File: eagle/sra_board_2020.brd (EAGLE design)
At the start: 81.4 x 109.8 mm, 45 parts, among them Q2 IRF9530, SW1 DTS-6, SW2 DTS-6, SW3 DTS-6, SW4 DTS-6, U1 ESP32-DEVKITC-32D, X1 057-006-1

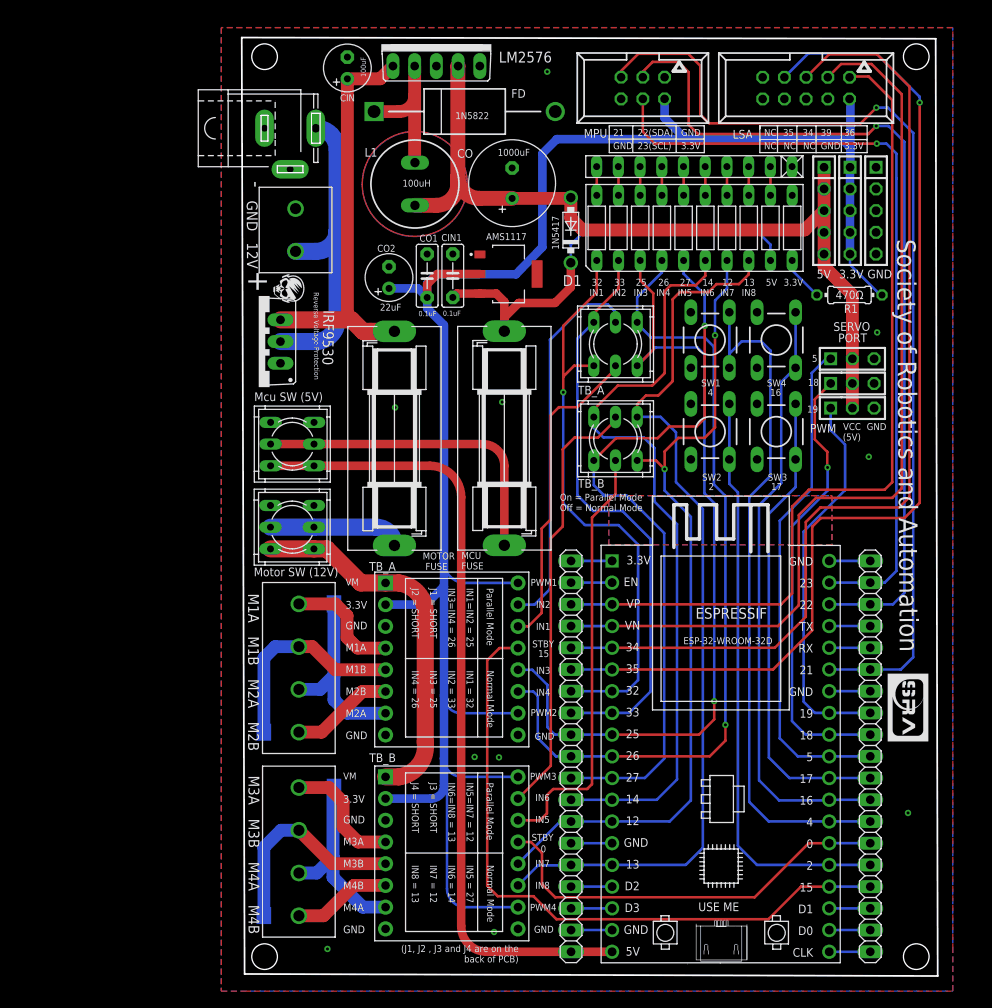
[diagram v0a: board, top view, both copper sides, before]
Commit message: Renamed Eagle files and Added Series Resistor Between ESP and Motor Driver
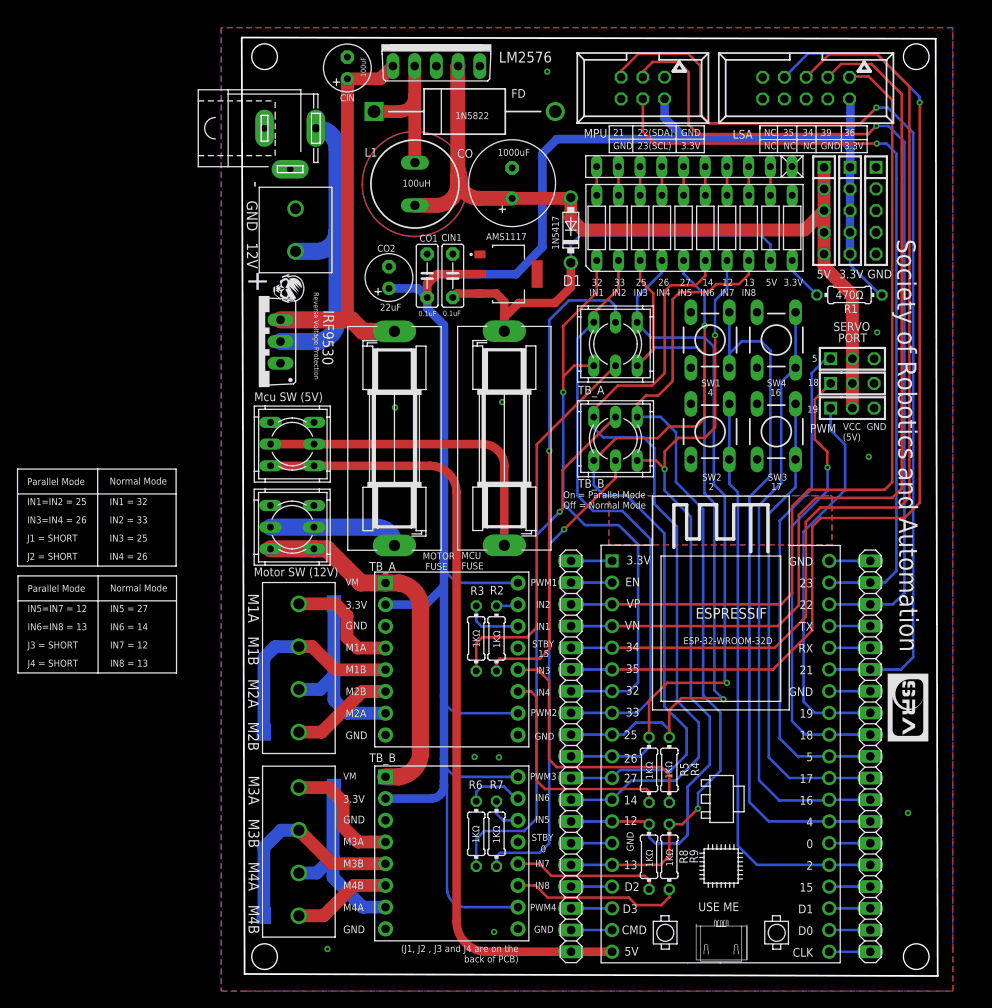
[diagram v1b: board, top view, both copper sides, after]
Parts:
- added R2, R3, R4, R5, R6, R7, R8, R9: 1KΩ, rcl:0204/7
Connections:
- new net N$10: R9.1, TB2.BIN2
- new net N$3: R2.1, TB1.AIN2
- new net N$4: R3.1, TB1.AIN1
- new net N$5: R4.1, TB1.BIN1
- new net N$6: R5.1, TB1.BIN2
- new net N$7: R6.1, TB2.AIN2
- new net N$8: R7.1, TB2.AIN1
- new net N$9: R8.1, TB2.BIN1
- net 12: now also R8.2; no longer TB2.BIN1
- net 13: now also R9.2; no longer TB2.BIN2
- net 15: no longer TB1.STBY
- net 25: now also R4.2; no longer TB1.BIN1
- net 26: now also R5.2; no longer TB1.BIN2
- net AIN1: now also R3.2; no longer TB1.AIN1
- net AIN2: now also R2.2; no longer TB1.AIN2
- net BIN1: now also R7.2; no longer TB2.AIN1
- net BIN2: now also R6.2; no longer TB2.AIN2
- net O: no longer TB2.STBY
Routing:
- net 15: track 78.6 -> 4.80 mm
- net O: track 48.6 -> 4.80 mm
- net N$5: track 0.00 -> 31.4 mm
- net N$6: track 0.00 -> 27.2 mm
- net AMS_IN: track 29.3 -> 50.4 mm
- net N$10: track 0.00 -> 19.9 mm
- net N$9: track 0.00 -> 17.2 mm
- net 26: track 96.4 -> 83.6 mm
- net AIN2: track 44.6 -> 57.2 mm, vias 0 -> 1
- net BIN2: track 51.0 -> 62.0 mm, vias 0 -> 1
- net AIN1: track 37.2 -> 45.5 mm
- net 25: track 95.7 -> 87.5 mm
- net N$4: track 0.00 -> 6.93 mm
- net N$7: track 0.00 -> 6.81 mm
- net 13: track 106.7 -> 100.4 mm, vias 0 -> 1
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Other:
- board text added: "CMD"

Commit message: Change the placement of Series Resistors and cleaned the routing
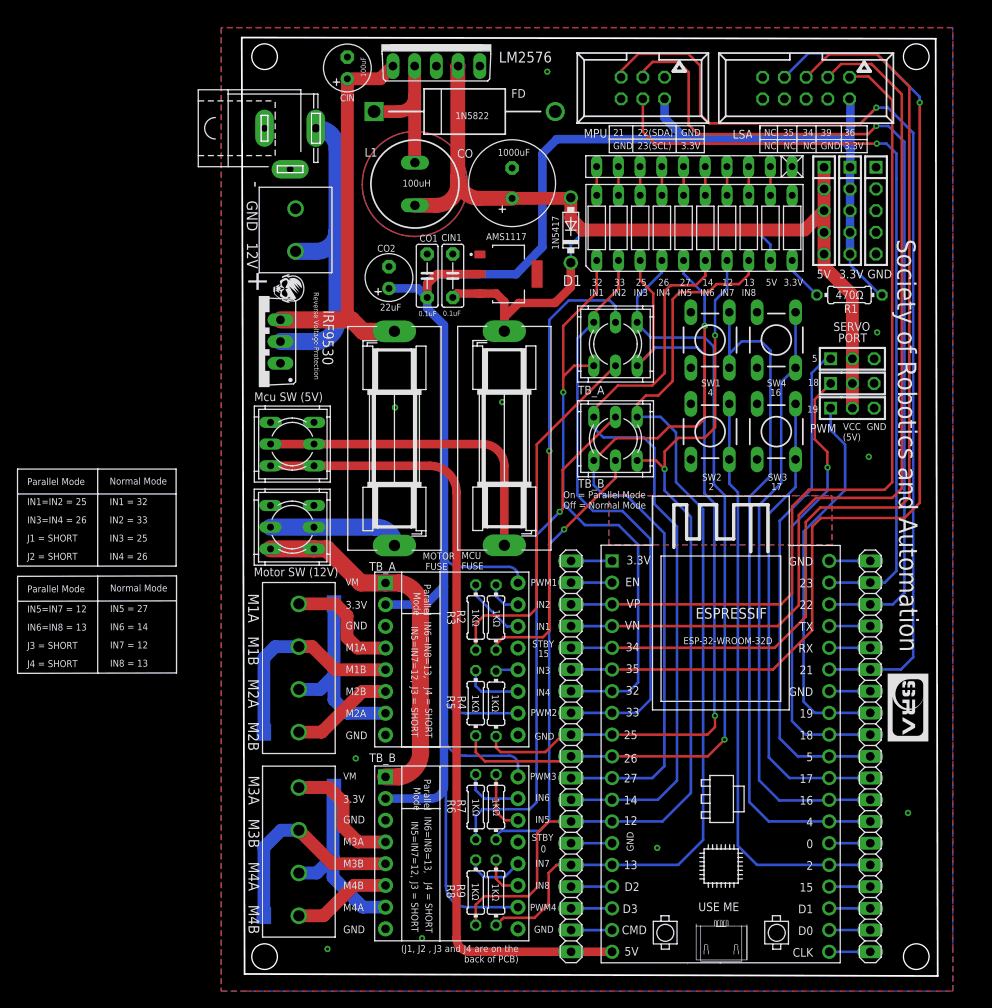
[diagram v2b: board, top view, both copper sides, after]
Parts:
- moved R5 21.7 mm to (27.9, 32.4), turned to 270 degrees
- moved R4 21.7 mm to (30.2, 32.4), turned to 270 degrees
- moved R8 20.7 mm to (27.9, 10.3), turned to 270 degrees
- moved R9 20.7 mm to (30.2, 10.3), turned to 270 degrees
- moved R6 3.13 mm to (27.9, 20.3)
- moved R7 3.13 mm to (30.2, 20.3)
- moved R2 2.45 mm to (30.2, 42.5)
- moved R3 2.45 mm to (27.9, 42.5)
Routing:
- net N$5: track 31.4 -> 2.64 mm
- net N$6: track 27.2 -> 7.01 mm
- net N$10: track 19.9 -> 5.10 mm
- net 26: track 83.6 -> 97.7 mm
- net 12: track 94.9 -> 108.7 mm
- net 13: track 100.4 -> 112.8 mm, vias 1 -> 0
- net N$9: track 17.2 -> 7.03 mm
- net 25: track 87.5 -> 95.3 mm
- net 3.3V: track 232.2 -> 238.0 mm
- net BIN1: track 56.0 -> 52.8 mm
- net N$8: track 4.29 -> 7.33 mm
- net 27: track 89.6 -> 86.7 mm
- net BIN2: track 62.0 -> 59.4 mm
- net AIN2: track 57.2 -> 54.8 mm
- net AIN1: track 45.5 -> 43.1 mm
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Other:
- board text added: "IN5=IN7=12,"
- board text added: "IN6=IN8=13,"

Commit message: Mosfet Replaced by two individual Diodes
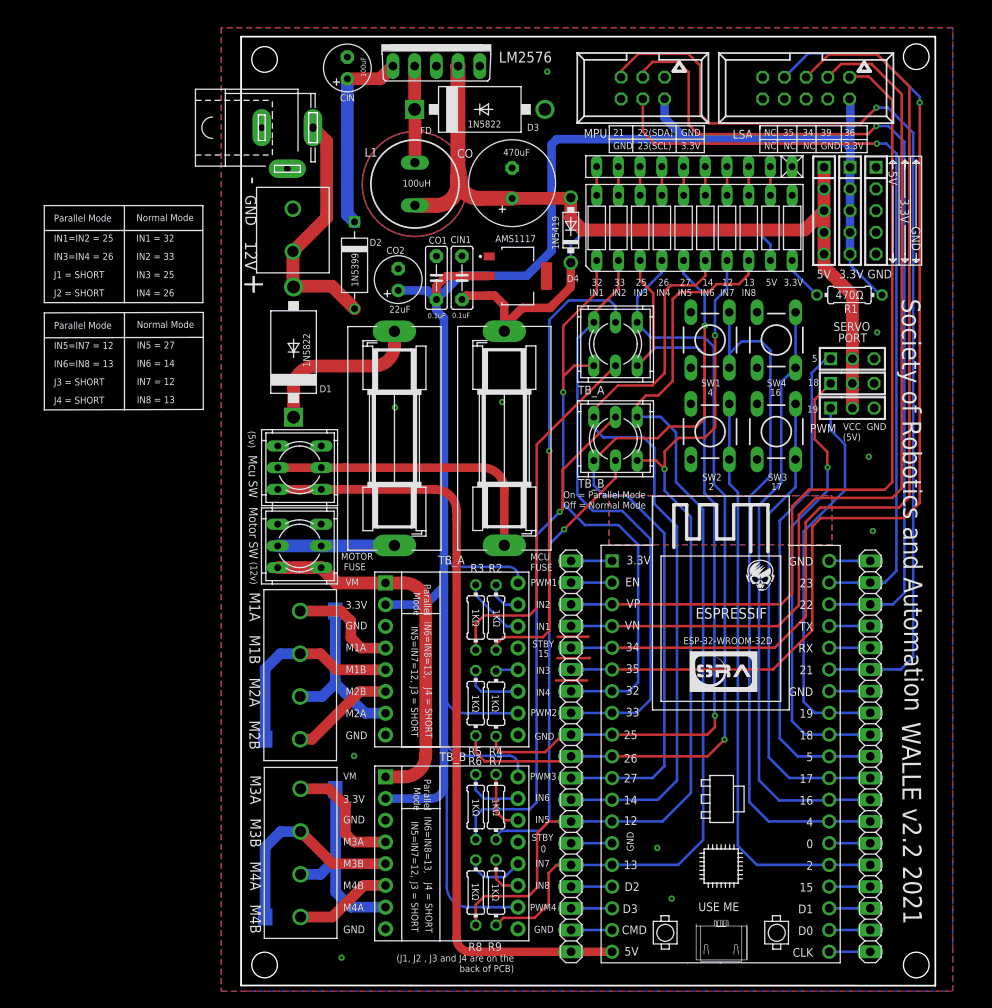
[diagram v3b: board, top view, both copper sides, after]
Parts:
- removed FD: 1N5822, 1N5822:DIOAD2120W130L950D530P
- removed Q2: IRF9530, transistor-power:TO220BV
- added U$1, U$2: 1N5399_SQUARE, diode_updated:C2673
- added U$3: 1N5399_ROUND, diode_updated:D-10
- CO: value 1000uF -> 470uF
- moved MCU-S/W 2.89 mm to (7.27, 60.0)
- moved MOTOR-S/W 2.35 mm to (7.26, 50.8)
- moved AMS1117 1.11 mm to (32.8, 82.4)
- moved CIN1 1.11 mm to (26.3, 82.2)
- moved CO1 1.11 mm to (23.3, 82.2)
- moved CO2 1.11 mm to (18.8, 82.0)
- moved J1 0.84 mm to (7.34, 35.7)
- moved PAD1 0.84 mm to (11.4, 43.2)
- moved PAD2 0.84 mm to (3.25, 28.2)
- moved POWER-JACK 0.34 mm to (5.84, 99.7)
- moved 12V 0.31 mm to (6.49, 87.8), turned to 270 degrees
- moved PAD3 0.31 mm to (11.4, 22.3)
- moved J2 0.25 mm to (7.39, 14.9)
- moved PAD4 0.23 mm to (3.24, 7.42)
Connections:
- removed net 12V: CIN.+, F3.1, JP6.1, Q2.S
- new net N$12: F3.1, U$1.C
- new net N$13: CIN.+, JP6.1, U$3.C
- net 0: now also 12V.1, U$2.A; no longer 12V.2, FD.A, Q2.G
- net 12V_U: now also 12V.2, U$1.A, U$3.A; no longer 12V.1, Q2.D
- net N$11: now also U$2.C; no longer FD.C
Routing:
- net 12V: track 50.9 -> 0.00 mm
- net N$13: track 0.00 -> 23.0 mm
- net N$12: track 0.00 -> 18.9 mm
- net 0: track 14.4 -> 25.4 mm
- net 12V_U: track 37.0 -> 29.3 mm
- net N$11: track 16.8 -> 11.4 mm
- net 5_AF: track 37.7 -> 34.1 mm
- net 5V_P: track 94.0 -> 90.8 mm
- net OUT3A: track 22.7 -> 20.5 mm
- net 3.3V: track 238.0 -> 236.2 mm
- net 12V_AF: track 15.4 -> 13.7 mm
- net OUT1A: track 13.8 -> 12.9 mm
- net OUT2A: track 24.6 -> 23.8 mm
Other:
- board size 81.4 x 109.8 mm -> 81.2 x 111 mm
- board text added: "(12v)"
- board text added: "(5v)"
- board text added: "1N5399"
- board text added: "1N5419"
- board text added: "1N5822"
- board text added: "D4"
- board text added: "FD"
- board text added: "Mcu SW"
- board text added: "Motor SW"
- board text added: "WALLE v2.2 2021"
- board text removed: "1N5417"
- board text removed: "Mcu SW (5V)"
- board text removed: "Motor SW (12V)"
- board text removed: "Reverse Voltage Protection"

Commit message: Front and back silkscreen improved
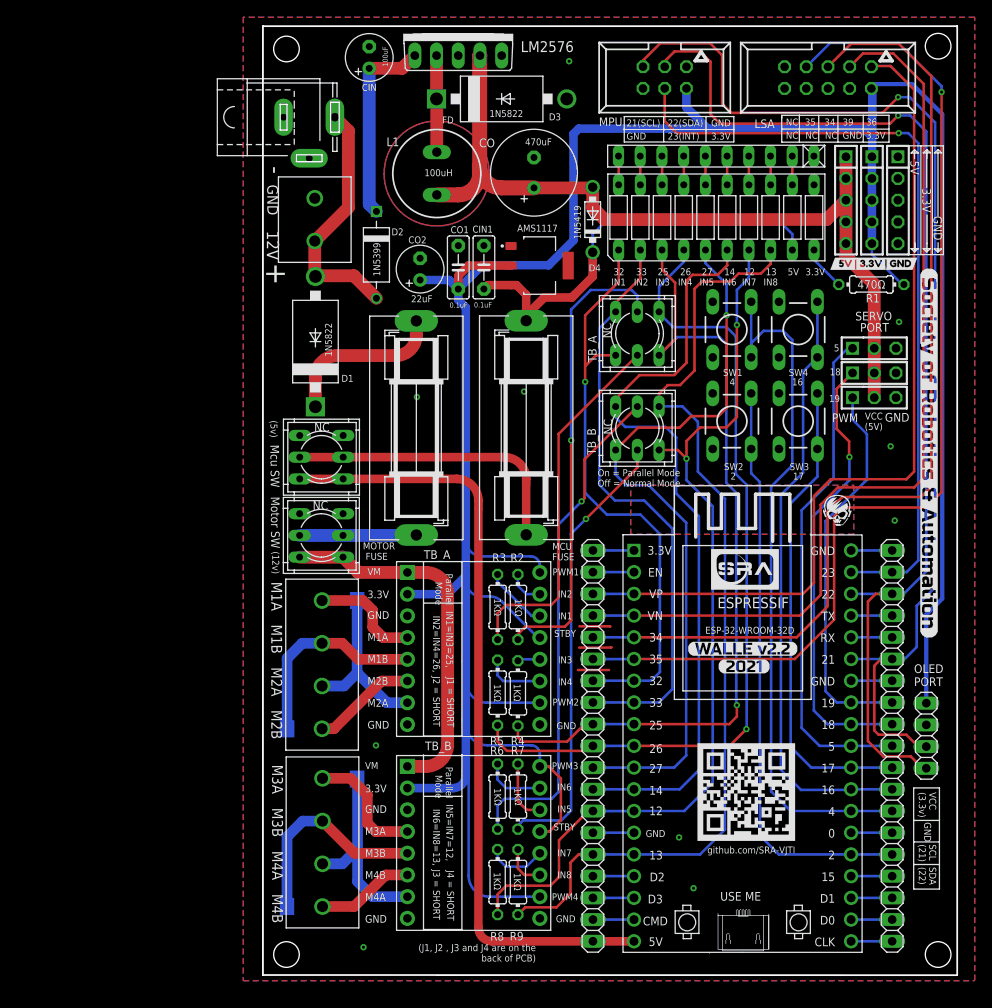
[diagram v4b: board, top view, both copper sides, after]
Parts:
- added OLED: (no value), pinhead:1X04
- moved SW1 2.84 mm to (57.8, 76.1)
- moved SW2 2.84 mm to (57.8, 65.4)
- moved SW3 2.84 mm to (65.6, 65.4)
- moved SW4 2.84 mm to (65.6, 76.1)
- moved 12V 2.84 mm to (9.05, 89.0)
- moved AMS1117 2.84 mm to (35.4, 83.6)
- moved CO 2.84 mm to (34.7, 94.5)
- moved RN2 2.84 mm to (56.0, 96.4)
- moved TB_A 2.84 mm to (46.8, 75.7)
- moved R6 2.84 mm to (30.4, 21.5)
- moved R8 2.84 mm to (30.4, 11.5)
- moved J1 2.84 mm to (9.90, 36.9)
- moved CIN1 2.84 mm to (28.8, 83.4)
- moved CO2 2.84 mm to (21.4, 83.2)
- moved F3 2.84 mm to (20.9, 64.6)
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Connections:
- net 0: now also OLED.2
- net 21: now also OLED.3
- net 22: now also OLED.4
- net 3.3V: now also OLED.1, TB1.STBY, TB2.STBY
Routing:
- net 3.3V: track 236.2 -> 338.0 mm
- net 22: track 102.1 -> 129.0 mm
- net 21: track 116.2 -> 131.8 mm
- net 12: track 108.7 -> 107.5 mm
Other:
- board text added: "21(SCL)"
- board text added: "23(INT)"
- board text added: "Designed By"
- board text added: "IN1=IN3=25,"
- board text added: "IN2=IN4=26,"
- board text added: "OLED PORT"
- board text added: "SCL (21)"
- board text added: "SDA (22)"
- board text added: "VCC (3.3v)"
- board text added: "github.com/SRA-VJTI"
- board text removed: "23(SCL)"
- board text removed: "IN1 = 32"
- board text removed: "IN1=IN2 = 25"
- board text removed: "IN2 = 33"
- board text removed: "IN3 = 25"
- board text removed: "IN3=IN4 = 26"
- board text removed: "IN4 = 26"
- board text removed: "IN5 = 27"
- board text removed: "IN5=IN7 = 12"
- board text removed: "IN6 = 14"
- board text removed: "IN6=IN8 = 13"
- board text removed: "IN7 = 12"
- board text removed: "IN8 = 13"
- board text removed: "J3"
- board text removed: "Normal Mode"
- board text removed: "Society of Robotics and Automation"
- board text removed: "WALLE v2.2 2021"
